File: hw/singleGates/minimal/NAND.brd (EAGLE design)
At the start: 5 parts, among them Q1 BC817, Q2 BC817

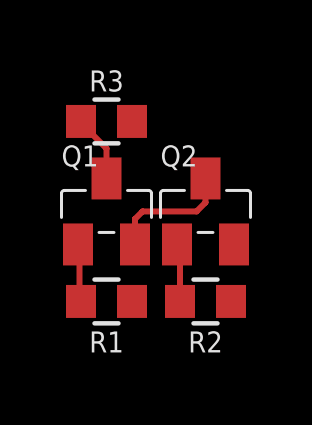
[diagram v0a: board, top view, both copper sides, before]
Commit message: Add led output and prepare first alu slice
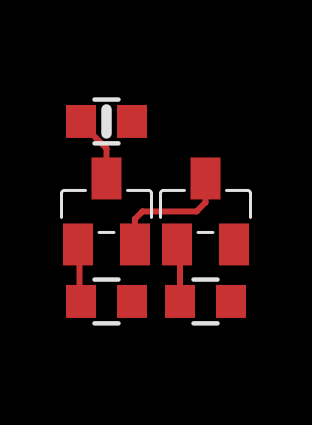
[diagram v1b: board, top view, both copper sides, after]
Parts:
- R3: device p.peter-gator:R0603 -> p.peter-rcl:R0603-MARK
